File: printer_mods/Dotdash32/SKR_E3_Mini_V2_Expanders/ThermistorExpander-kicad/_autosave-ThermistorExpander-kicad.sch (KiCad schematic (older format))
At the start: 8 parts, among them J1 SPI1_breakaway, J2 JST-XH2, J3 JST-XH2, J4 JST-XH2

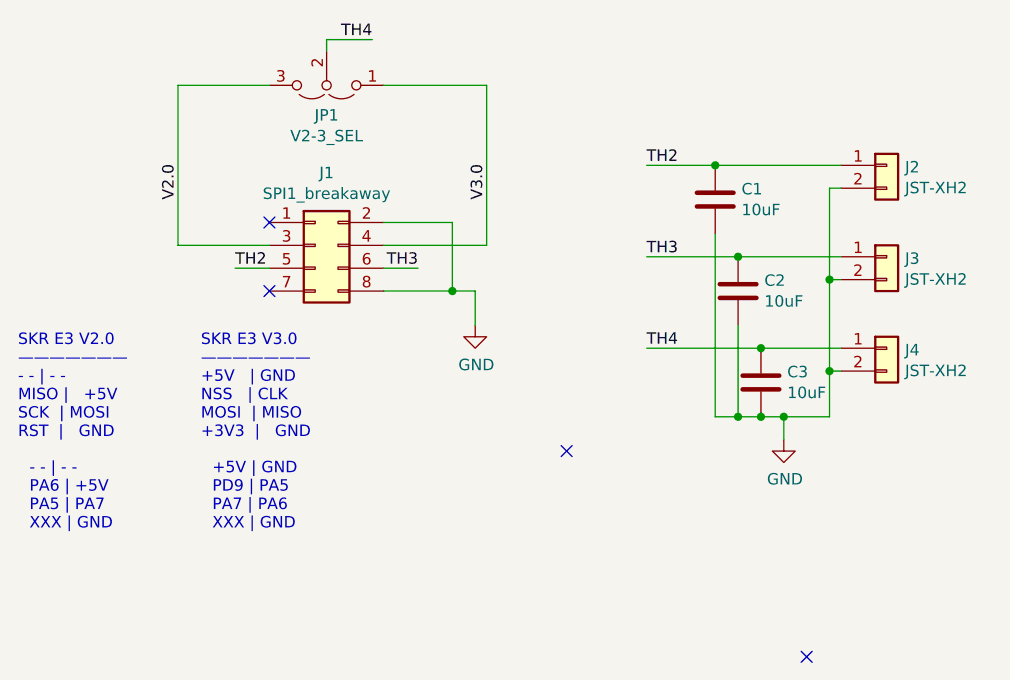
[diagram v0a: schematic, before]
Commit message: feat|docs: 2x4 SPI header, readme updates
also re-routing some silly decisions, cleaning schematic
Also moving some readme-stuff around for
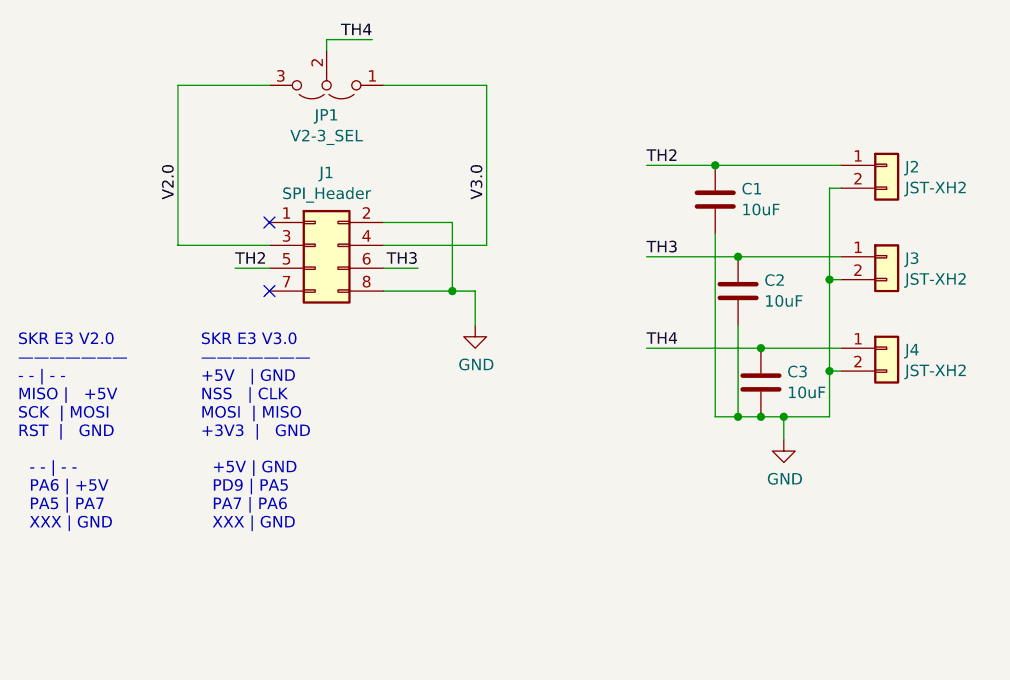
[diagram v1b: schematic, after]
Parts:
- J1: value SPI1_breakaway -> SPI_Header
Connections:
- no-connect marks 4 -> 2
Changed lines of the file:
@@
 P 2250 1950
 F 0 "J1" H 2300 2267 50  0000 C CNN
-F 1 "SPI1_breakaway" H 2300 2176 50  0000 C CNN
+F 1 "SPI_Header" H 2300 2176 50  0000 C CNN
 F 2 "Pin_Headers:Pin_Header_Straight_2x04_Pitch2.54mm" H 2250 1950 50  0001 C CNN
 F 3 "~" H 2250 1950 50  0001 C CNN
@@
 NoConn ~ 2050 2150
 NoConn ~ 2050 1850
-NoConn ~ 3350 2850
-NoConn ~ 4400 3750
 $EndSCHEMATC
